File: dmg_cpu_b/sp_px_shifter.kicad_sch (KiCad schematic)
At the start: 89 parts

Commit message: All sheets captured. Serious tidying is required in PPU section.
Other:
- company: (none) -> CC-BY-SA-4.0 Régis Galland & Michael Singer -- Derived work from Furrtek
- title: (none) -> DMG CPU B
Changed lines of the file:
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@@
 (kicad_sch (version 20211123) (generator eeschema)
   (paper "A3")
+  (title_block
+    (title "DMG CPU B")
+    (date "2022-05-19")
+    (rev "0")
+    (company "CC-BY-SA-4.0 Régis Galland & Michael Singer -- Derived work from Furrtek")
+    (comment 1 "https://github.com/msinger/dmg-schematics")
+  )
   (junction (at 256.54 168.275) (diameter 0) (color 0 0 0 0)
   )

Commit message: Fixes based on review. + various other edits.
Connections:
- net TEXY renamed SP_BP_CYS
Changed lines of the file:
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@@
     (effects (font (size 1.27 1.27)) (justify right))
   )
-  (hierarchical_label "TEXY" (shape input) (at 33.655 47.625 180)
+  (hierarchical_label "SP_BP_CYS" (shape input) (at 33.655 47.625 180)
     (effects (font (size 1.27 1.27)) (justify right))
   )

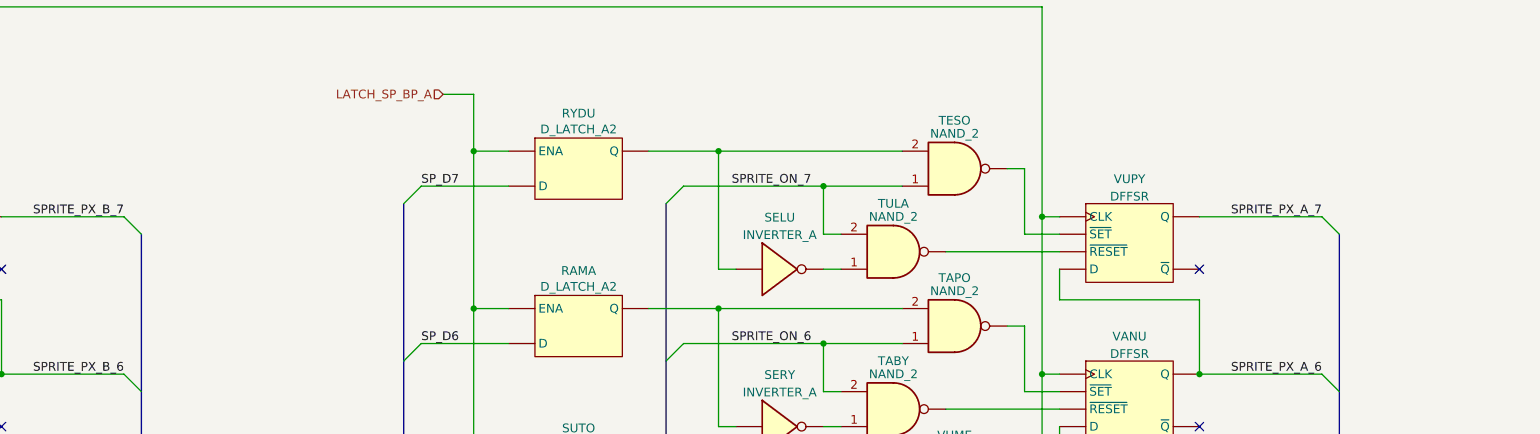
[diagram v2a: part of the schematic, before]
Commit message: All connections between sheet are complete. Can still do with a good tidy up.
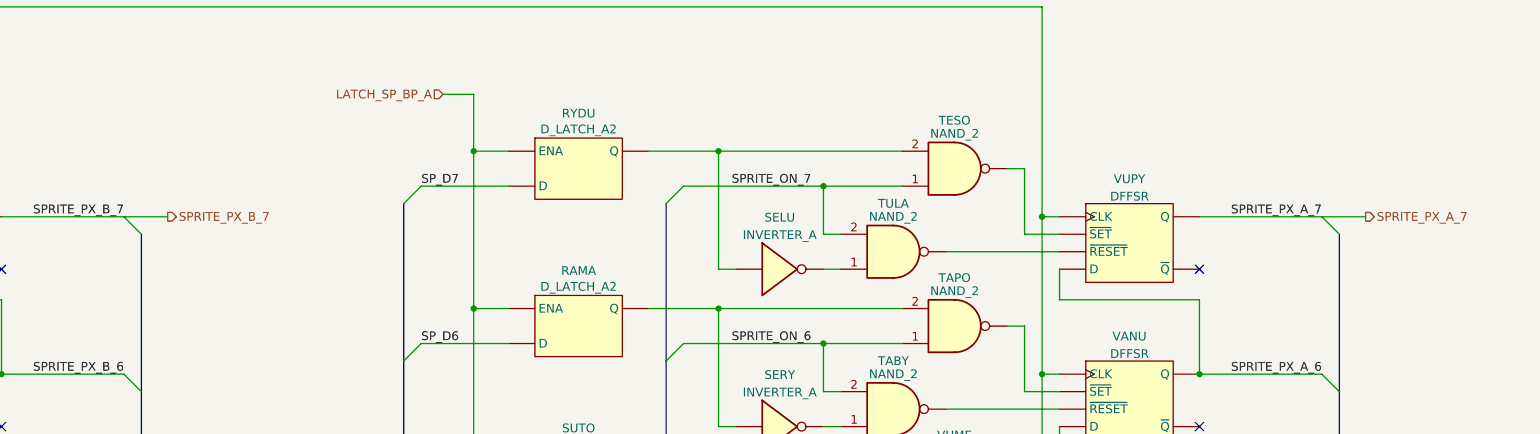
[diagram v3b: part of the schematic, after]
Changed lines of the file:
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@@
+    (stroke (width 0) (type default) (color 0 0 0 0))
+  )
+  (wire (pts (xy 379.73 63.5) (xy 386.08 63.5))
     (stroke (width 0) (type default) (color 0 0 0 0))
   )
@@
     (stroke (width 0) (type default) (color 0 0 0 0))
   )
+  (wire (pts (xy 205.74 63.5) (xy 212.09 63.5))
+    (stroke (width 0) (type default) (color 0 0 0 0))
+  )
   (wire (pts (xy 307.34 180.34) (xy 307.34 173.355))
     (stroke (width 0) (type default) (color 0 0 0 0))
@@
   (label "SPRITE_PX_B_5" (at 205.74 109.22 180)
     (effects (font (size 1.27 1.27)) (justify right bottom))
+  )
+  (hierarchical_label "SPRITE_PX_B_7" (shape output) (at 212.09 63.5 0)
+    (effects (font (size 1.27 1.27)) (justify left))
   )
   (hierarchical_label "LATCH_SP_BP_B" (shape input) (at 78.105 45.72 180)
@@
   )
   (hierarchical_label "SPRITE_PX_A_[0..7]" (shape output) (at 385.445 230.505 0)
+    (effects (font (size 1.27 1.27)) (justify left))
+  )
+  (hierarchical_label "SPRITE_PX_A_7" (shape output) (at 386.08 63.5 0)
     (effects (font (size 1.27 1.27)) (justify left))
   )
@@
   (symbol (lib_id "power:GND") (at 167.64 233.68 0) (unit 1)
     (in_bom yes) (on_board yes) (fields_autoplaced)
-    (property "Reference" "#PWR?" (id 0) (at 167.64 240.03 0)
+    (property "Reference" "#PWR0125" (id 0) (at 167.64 240.03 0)
       (effects (font (size 1.27 1.27)) hide)
     )
@@
   (symbol (lib_id "power:GND") (at 341.63 233.68 0) (unit 1)
     (in_bom yes) (on_board yes) (fields_autoplaced)
-    (property "Reference" "#PWR?" (id 0) (at 341.63 240.03 0)
-      (effects (font (size 1.27 1.27)) hide)
-    )
+    (property "Reference" "#PWR0126" (id 0) (at 341.63 240.03 0)
+      (effects (font (size 1.27 1.27)) hide)
+    )

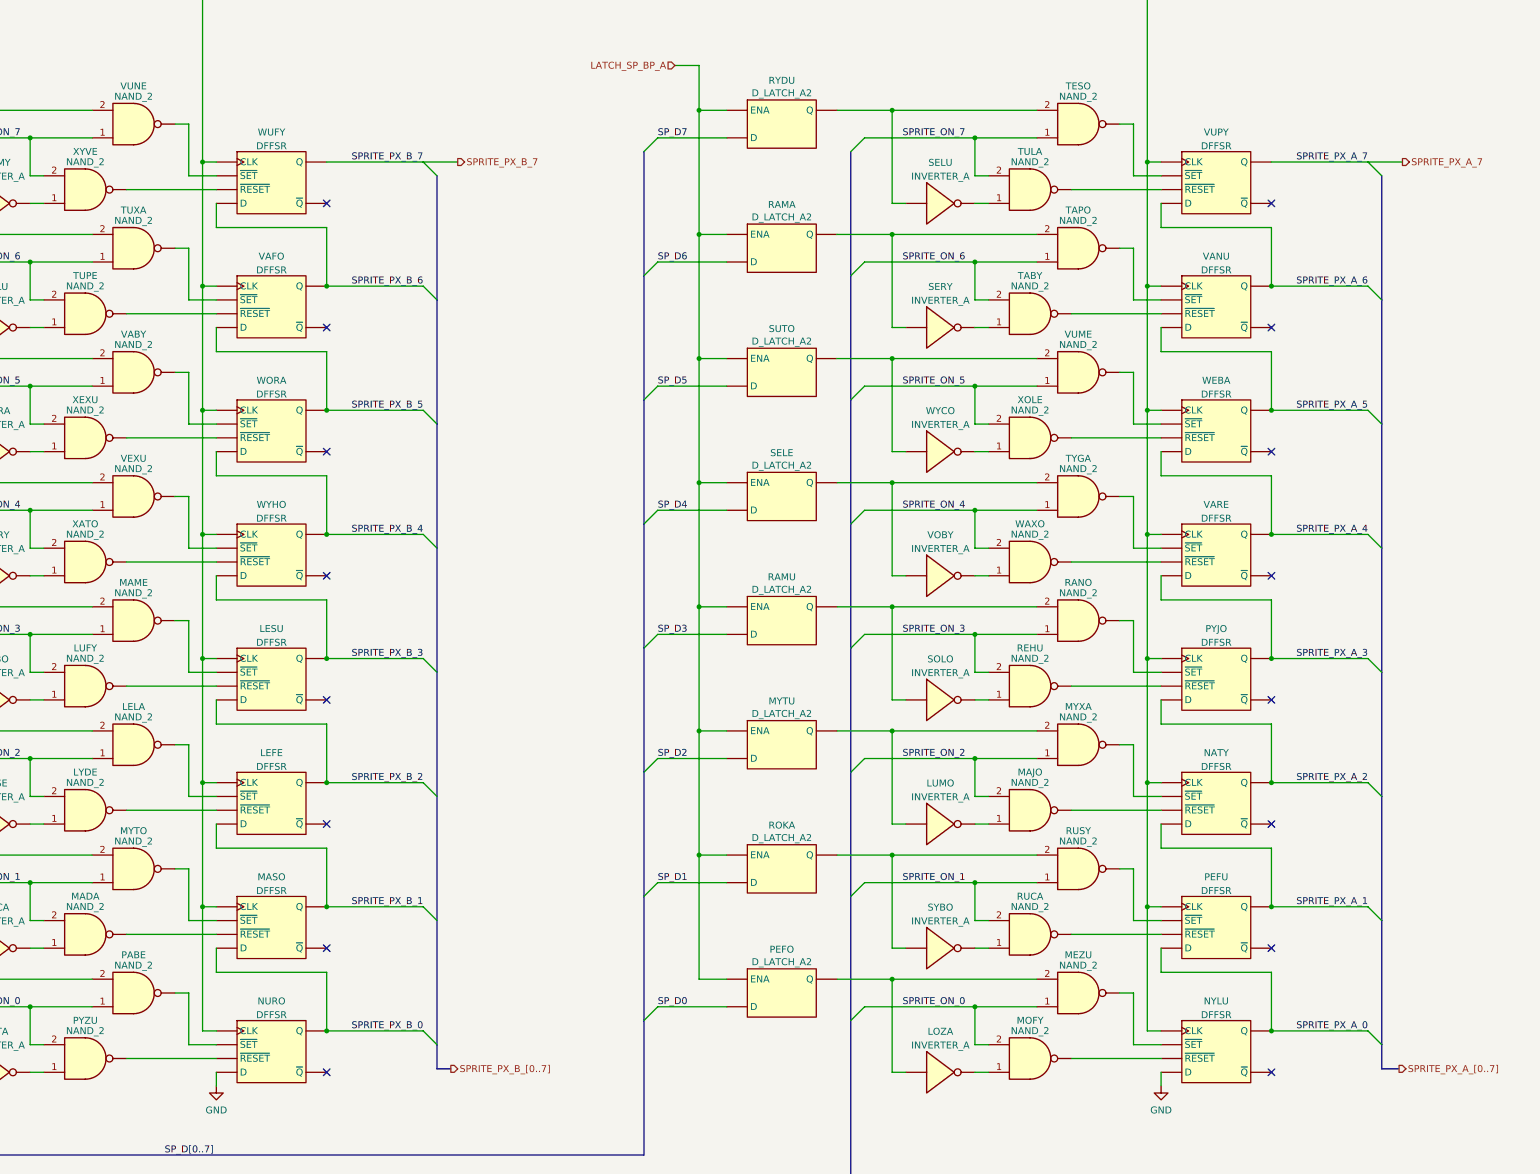
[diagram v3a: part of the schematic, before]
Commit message: Quite a few fixes from review.
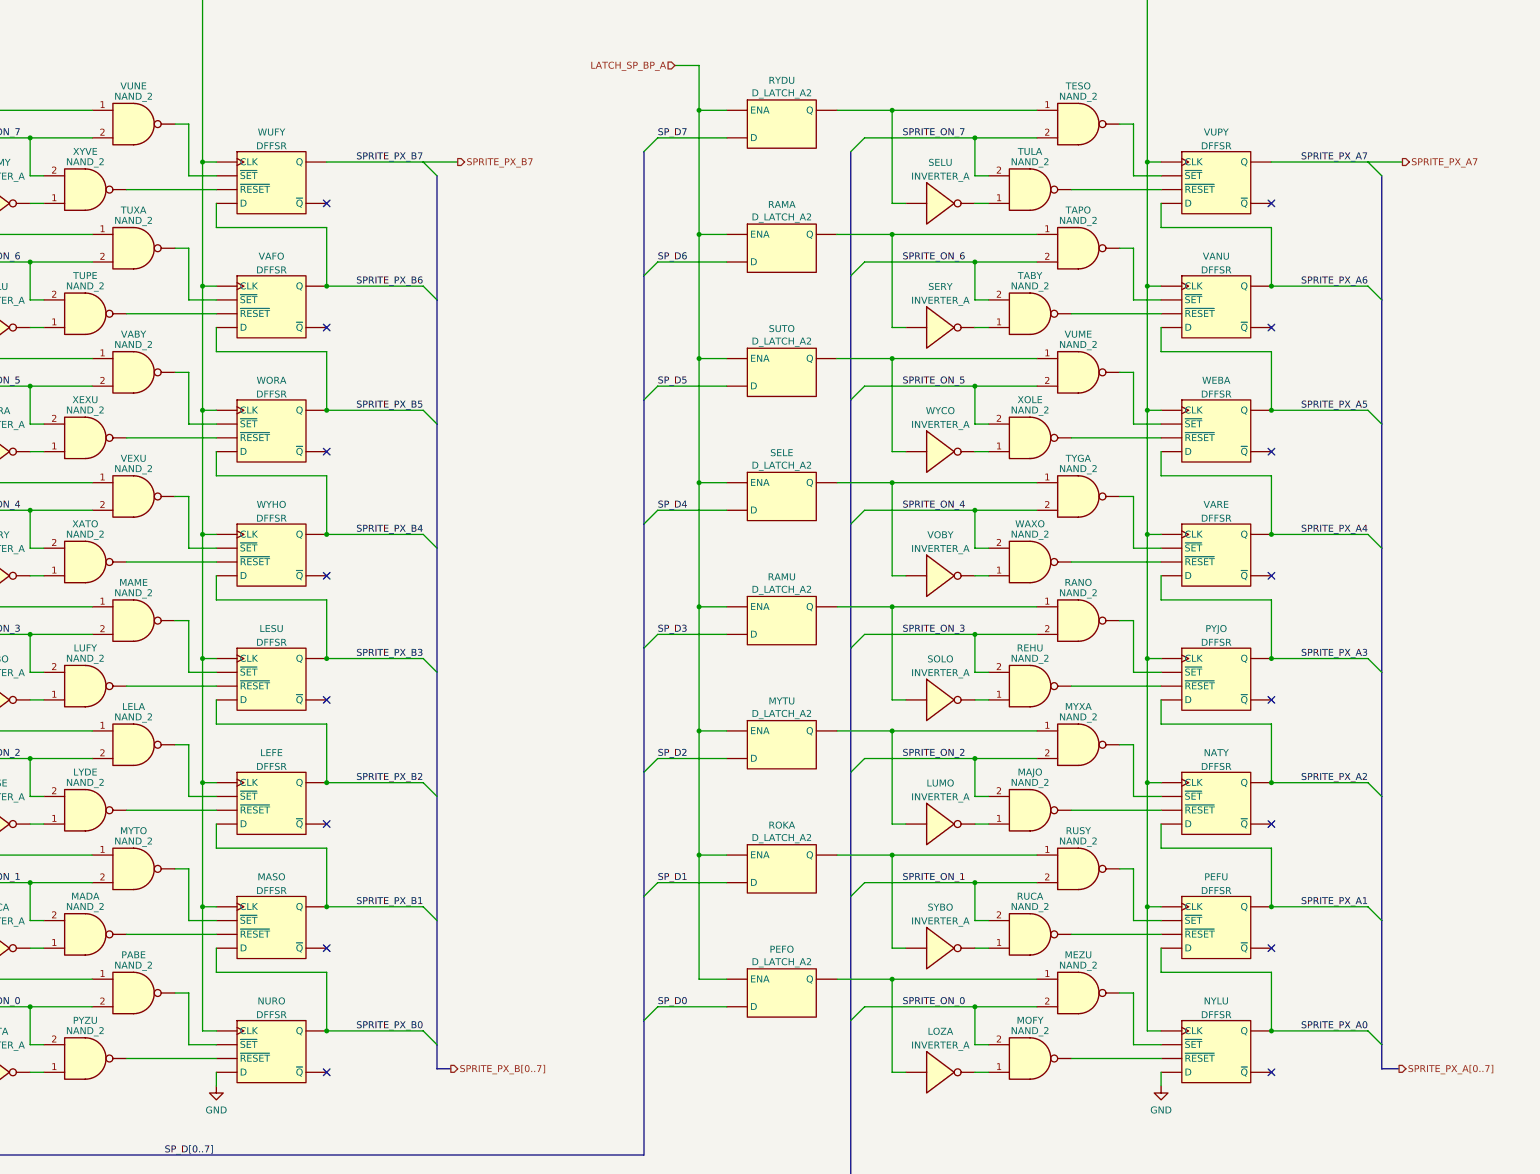
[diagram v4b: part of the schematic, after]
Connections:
- net SPRITE_ON_0: now also MEZU.2, PABE.2; no longer MEZU.1, PABE.1
- net SPRITE_ON_1: now also MYTO.2, RUSY.2; no longer MYTO.1, RUSY.1
- net SPRITE_ON_2: now also LELA.2, MYXA.2; no longer LELA.1, MYXA.1
- net SPRITE_ON_3: now also MAME.2, RANO.2; no longer MAME.1, RANO.1
- net SPRITE_ON_4: now also TYGA.2, VEXU.2; no longer TYGA.1, VEXU.1
- net SPRITE_ON_5: now also VABY.2, VUME.2; no longer VABY.1, VUME.1
- net SPRITE_ON_6: now also TAPO.2, TUXA.2; no longer TAPO.1, TUXA.1
- net SPRITE_ON_7: now also TESO.2, VUNE.2; no longer TESO.1, VUNE.1
- net at ROKA.4 (Q), SYBO.1: now also RUSY.1; no longer RUSY.2
- net at LUMO.1, MYTU.4 (Q): now also MYXA.1; no longer MYXA.2
- net at LASE.1, MOFO.4 (Q): now also LELA.1; no longer LELA.2
- net at NUCA.1, PEBA.4 (Q): now also MYTO.1; no longer MYTO.2
- net at RYDU.4 (Q), SELU.1: now also TESO.1; no longer TESO.2
- net at SAJA.4 (Q), WERY.1: now also VEXU.1; no longer VEXU.2
- net at RAMA.4 (Q), SERY.1: now also TAPO.1; no longer TAPO.2
- net at SUTO.4 (Q), WYCO.1: now also VUME.1; no longer VUME.2
- net at SEMO.4 (Q), SULU.1: now also TUXA.1; no longer TUXA.2
- net at LOZA.1, PEFO.4 (Q): now also MEZU.1; no longer MEZU.2
- net at LUBO.1, PUDU.4 (Q): now also MAME.1; no longer MAME.2
- net at RAMU.4 (Q), SOLO.1: now also RANO.1; no longer RANO.2
- net at SUNY.4 (Q), WURA.1: now also VABY.1; no longer VABY.2
- net at SELE.4 (Q), VOBY.1: now also TYGA.1; no longer TYGA.2
- net at SEGA.4 (Q), WAMY.1: now also VUNE.1; no longer VUNE.2
- net at RATA.1, REWO.4 (Q): now also PABE.1; no longer PABE.2
- net SPRITE_PX_A_0 renamed SPRITE_PX_A0
- net SPRITE_PX_A_1 renamed SPRITE_PX_A1
- net SPRITE_PX_A_2 renamed SPRITE_PX_A2
- net SPRITE_PX_A_3 renamed SPRITE_PX_A3
- net SPRITE_PX_A_4 renamed SPRITE_PX_A4
- net SPRITE_PX_A_5 renamed SPRITE_PX_A5
- net SPRITE_PX_A_6 renamed SPRITE_PX_A6
- net SPRITE_PX_A_7 renamed SPRITE_PX_A7
- net SPRITE_PX_B_0 renamed SPRITE_PX_B0
- net SPRITE_PX_B_1 renamed SPRITE_PX_B1
- net SPRITE_PX_B_2 renamed SPRITE_PX_B2
- net SPRITE_PX_B_3 renamed SPRITE_PX_B3
- net SPRITE_PX_B_4 renamed SPRITE_PX_B4
- net SPRITE_PX_B_5 renamed SPRITE_PX_B5
- net SPRITE_PX_B_6 renamed SPRITE_PX_B6
- net SPRITE_PX_B_7 renamed SPRITE_PX_B7
